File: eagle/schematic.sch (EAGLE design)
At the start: 15 parts, among them Q3 TIP120, Q4 TIP120

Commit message: Update scehmatic with pull up resistors and closer resistor values
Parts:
- removed UNION1, UNION2: SOLDERJUMPERTRACE, SparkFun-Retired:SOLDERJUMPERTRACE
- added R5: 1.8K, SparkFun-Resistors:1KOHM-HORIZ-1/4W-1%
- added R6: 5K, SparkFun-Resistors:1KOHM-HORIZ-1/4W-1%
- added UNION_ARDUINO_GND_9V-, UNION_ARDUINO_VIN_9V+: SOLDERJUMPERTRACE, SparkFun-Retired:SOLDERJUMPERTRACE
- J1: device SparkFun-Connectors:CONN_04 -> SparkFun-Connectors:CONN_06SILK_FEMALE_PTH
- J3: device SparkFun-Connectors:CONN_06SILK_FEMALE_PTH -> SparkFun-Connectors:CONN_04
- R2: value 1k -> 0.4k
- R3: value 1k -> 0.4K
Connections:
- net 9V+: now also J1.6, UNION_ARDUINO_VIN_9V+.2; no longer J3.6, UNION1.2
- net 9V-: now also J1.5, UNION_ARDUINO_GND_9V-.2; no longer J3.5, UNION2.2
- net ARDUINO_5V: now also J3.2, R6.2; no longer J2.2
- net ARDUINO_GND: now also J1.3, J3.1, UNION_ARDUINO_GND_9V-.1; no longer J2.1, J3.3, UNION2.1
- net ARDUINO_RX: now also J3.3; no longer J2.3
- net ARDUINO_TX: now also J3.4; no longer J2.4
- net ARDUINO_VIN: now also J1.4, UNION_ARDUINO_VIN_9V+.1; no longer J3.4, UNION1.1
- net FIRE_GATE: now also J1.2; no longer J3.2
- net JETSON_1.8V: now also J2.2, R5.2; no longer J1.2
- net JETSON_GND: now also J2.1; no longer J1.1
- net JETSON_RX: now also J2.3; no longer J1.3
- net JETSON_TX: now also J2.4; no longer J1.4
- net N: now also R5.1
- net N2: now also R6.1
- net SPIN_ENABLE: now also J1.1; no longer J3.1
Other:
- note added: "Headers"
- note added: "Net Unions"
- note removed: "Isolation (9600 BAUD UART)"

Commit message: Update schematic
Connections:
- removed net FIRE_GATE: J1.2
- net FIRE_ENABLE: now also J1.2
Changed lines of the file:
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@@
 <segment>
 <pinref part="OK2" gate="A" pin="C"/>
-<wire x1="2.54" y1="15.24" x2="-5.08" y2="12.7" width="0.1524" layer="91"/>
-<label x="-5.08" y="12.7" size="1.778" layer="95" rot="R180" xref="yes"/>
+<wire x1="2.54" y1="15.24" x2="-17.78" y2="15.24" width="0.1524" layer="91"/>
+<label x="-17.78" y="15.24" size="1.778" layer="95" rot="R180" xref="yes"/>
 </segment>
 </net>
@@
 <segment>
 <pinref part="OK1" gate="A" pin="C"/>
-<wire x1="2.54" y1="45.72" x2="-5.08" y2="43.18" width="0.1524" layer="91"/>
-<label x="-5.08" y="43.18" size="1.778" layer="95" rot="R180" xref="yes"/>
+<wire x1="2.54" y1="45.72" x2="-20.32" y2="45.72" width="0.1524" layer="91"/>
+<label x="-20.32" y="45.72" size="1.778" layer="95" rot="R180" xref="yes"/>
 </segment>
 </net>
@@
 <segment>
 <pinref part="OK1" gate="A" pin="EMIT"/>
-<wire x1="20.32" y1="45.72" x2="27.94" y2="43.18" width="0.1524" layer="91"/>
-<label x="27.94" y="43.18" size="1.778" layer="95" xref="yes"/>
+<wire x1="20.32" y1="45.72" x2="38.1" y2="45.72" width="0.1524" layer="91"/>
+<label x="38.1" y="45.72" size="1.778" layer="95" xref="yes"/>
 </segment>
 </net>
@@
 <segment>
 <pinref part="OK2" gate="A" pin="EMIT"/>
-<wire x1="20.32" y1="15.24" x2="27.94" y2="12.7" width="0.1524" layer="91"/>
-<label x="27.94" y="12.7" size="1.778" layer="95" xref="yes"/>
+<wire x1="20.32" y1="15.24" x2="38.1" y2="15.24" width="0.1524" layer="91"/>
+<label x="38.1" y="15.24" size="1.778" layer="95" xref="yes"/>
 </segment>
 </net>
@@
 </segment>
 </net>
-<net name="FIRE_GATE" class="0">
+<net name="FIRE_ENABLE" class="0">
 <segment>
 <pinref part="J1" gate="G$1" pin="2"/>

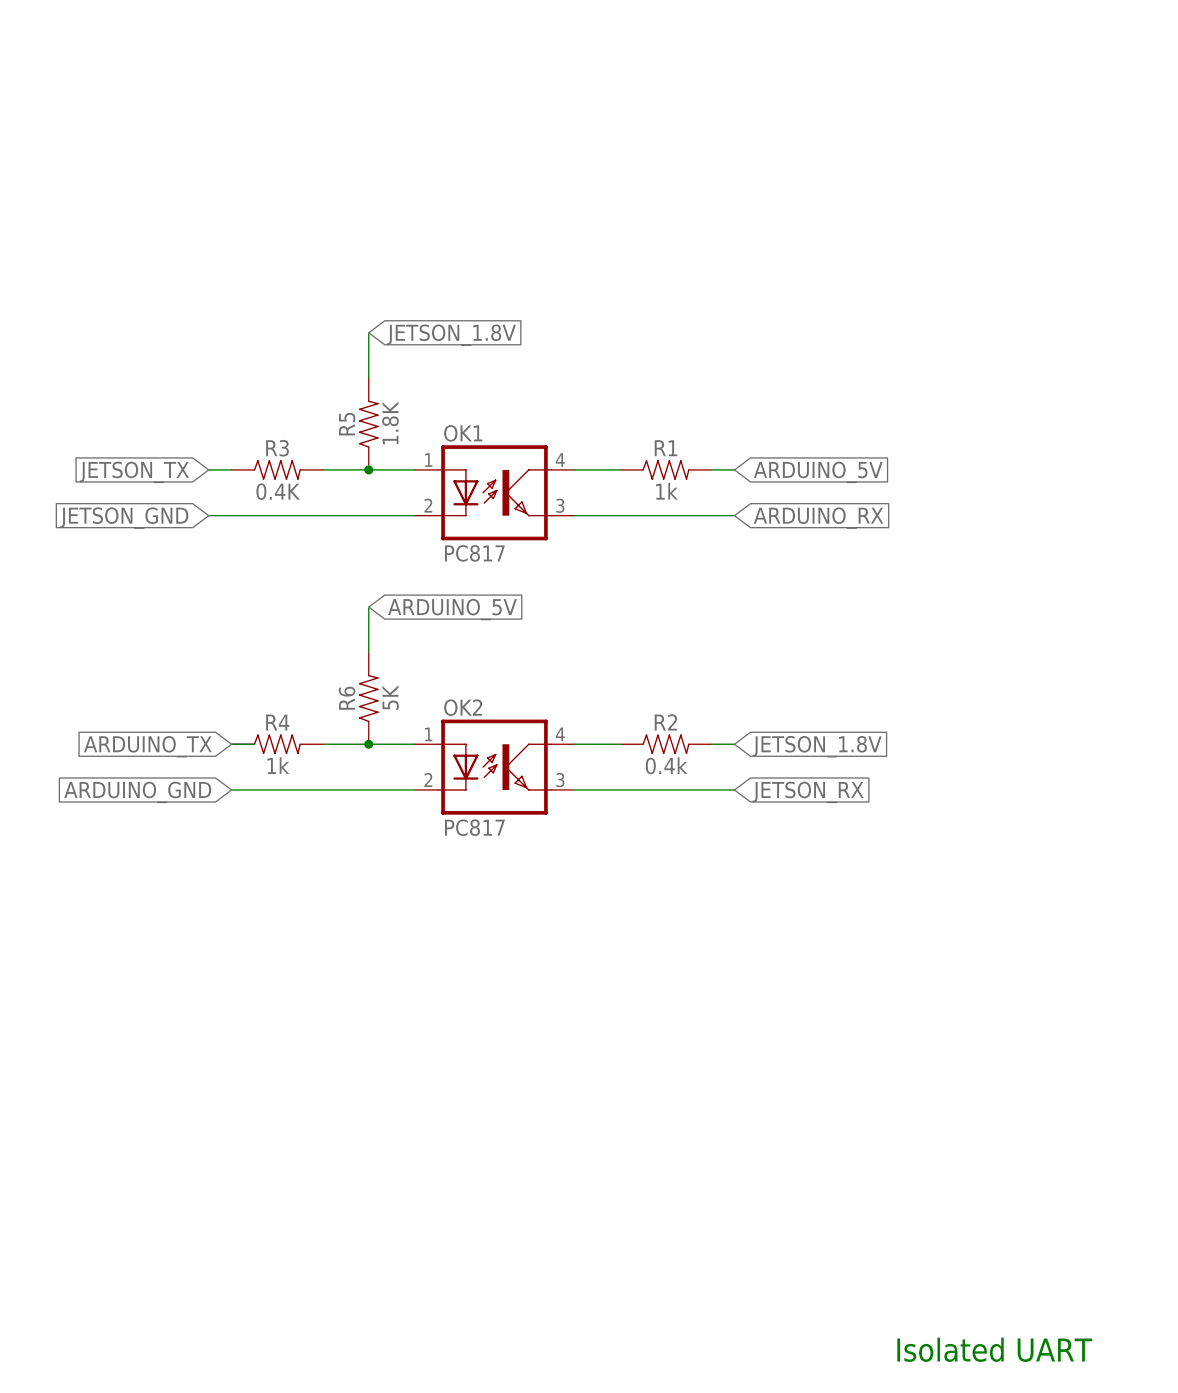
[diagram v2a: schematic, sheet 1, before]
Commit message: Update schematic with working optocoupler communication schematic
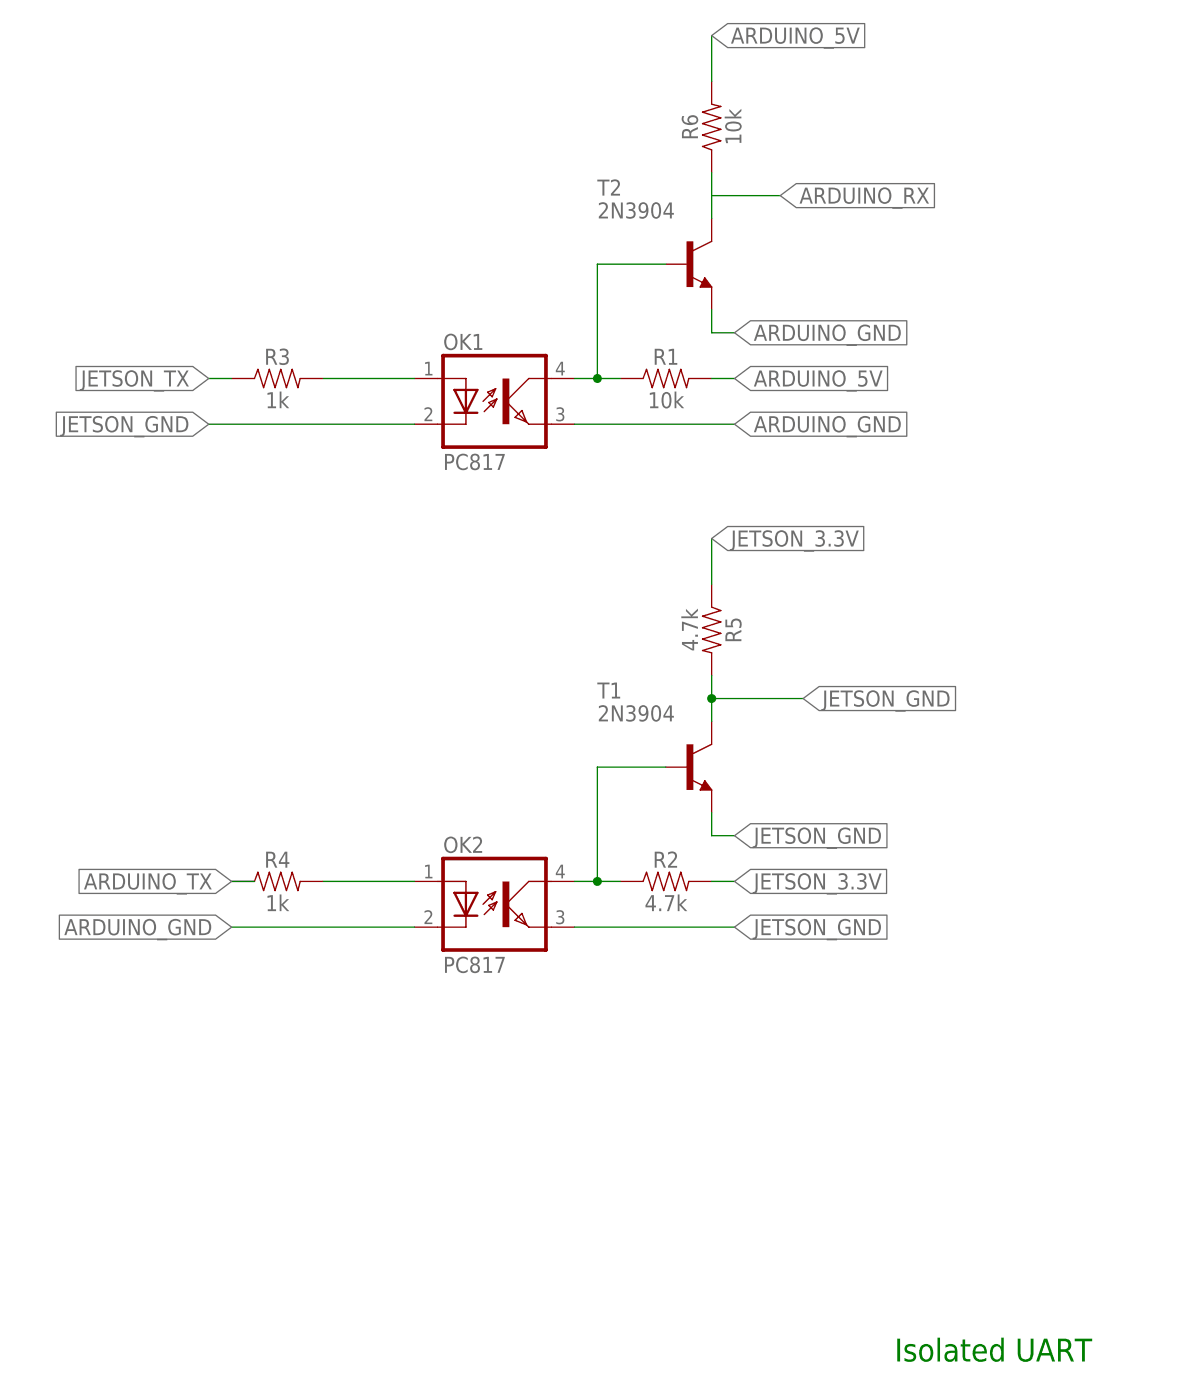
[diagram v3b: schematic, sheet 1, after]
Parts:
- added T1, T2: 2N3904, transistor:2N3904
- R1: value 1k -> 10k
- R2: value 0.4k -> 4.7k
- R3: value 0.4K -> 1k
- R5: value 1.8K -> 4.7k
- R6: value 5K -> 10k
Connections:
- removed net JETSON_1.8V: J2.2, R2.2, R5.2
- new net JETSON_3.3V: J2.2, R2.2, R5.1
- net ARDUINO_GND: now also OK1.EMIT, T2.E
- net ARDUINO_RX: now also R6.1, T2.C; no longer OK1.EMIT
- net JETSON_GND: now also OK2.EMIT, R5.2, T1.C, T1.E
- net JETSON_RX: no longer OK2.EMIT
- net N: no longer R5.1
- net N$3: now also T1.B
- net N$4: now also T2.B
- net N2: no longer R6.1
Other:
- moved on the sheet: OK1, OK2, R1, R2, R3, R4, R5, R6

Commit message: Update schematic
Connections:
- net FIRE_ENABLE renamed CYCLE_ENABLE
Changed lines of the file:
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@@
 </segment>
 </net>
-<net name="FIRE_ENABLE" class="0">
+<net name="CYCLE_ENABLE" class="0">
 <segment>
 <pinref part="Q3" gate="1" pin="B"/>
@@
 </segment>
 </net>
-<net name="FIRE_ENABLE" class="0">
+<net name="CYCLE_ENABLE" class="0">
 <segment>
 <pinref part="J1" gate="G$1" pin="2"/>

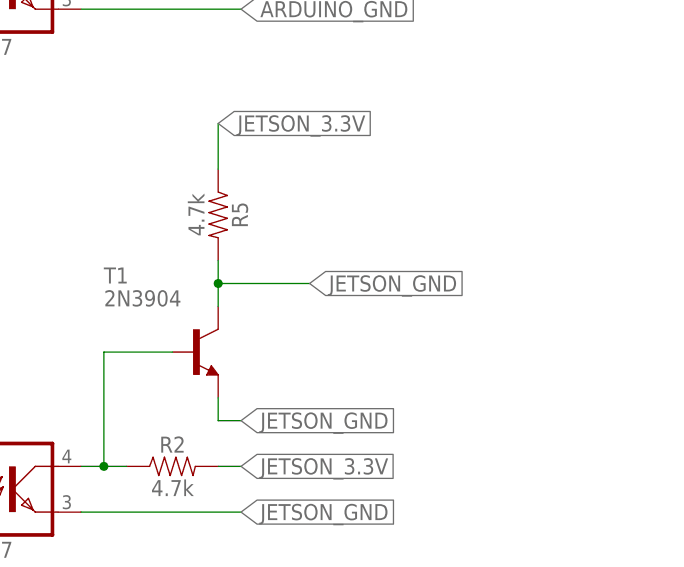
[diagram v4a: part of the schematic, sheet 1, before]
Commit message: Correct wrong net in isolated UART circuit
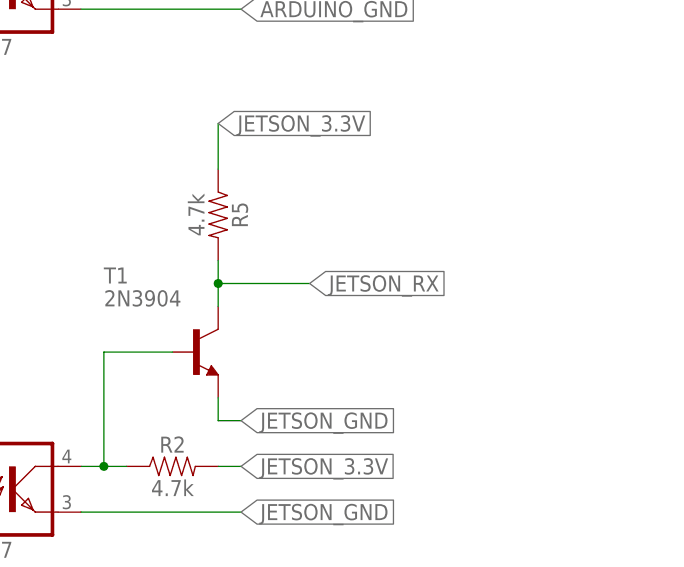
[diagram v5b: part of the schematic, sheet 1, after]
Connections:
- net JETSON_GND: no longer R5.2, T1.C
- net JETSON_RX: now also R5.2, T1.C
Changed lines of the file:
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@@
-</segment>
-<segment>
-<pinref part="R5" gate="G$1" pin="2"/>
-<pinref part="T1" gate="G1" pin="C"/>
-<wire x1="35.56" y1="27.94" x2="35.56" y2="25.4" width="0.1524" layer="91"/>
-<wire x1="35.56" y1="25.4" x2="35.56" y2="22.86" width="0.1524" layer="91"/>
-<wire x1="35.56" y1="25.4" x2="45.72" y2="25.4" width="0.1524" layer="91"/>
-<junction x="35.56" y="25.4"/>
-<label x="45.72" y="25.4" size="1.778" layer="95" xref="yes"/>
 </segment>
 <segment>
@@
 </segment>
 </net>
+<net name="JETSON_RX" class="0">
+<segment>
+<pinref part="R5" gate="G$1" pin="2"/>
+<pinref part="T1" gate="G1" pin="C"/>
+<wire x1="35.56" y1="27.94" x2="35.56" y2="25.4" width="0.1524" layer="91"/>
+<wire x1="35.56" y1="25.4" x2="35.56" y2="22.86" width="0.1524" layer="91"/>
+<wire x1="35.56" y1="25.4" x2="45.72" y2="25.4" width="0.1524" layer="91"/>
+<junction x="35.56" y="25.4"/>
+<label x="45.72" y="25.4" size="1.778" layer="95" xref="yes"/>
+</segment>
+</net>
